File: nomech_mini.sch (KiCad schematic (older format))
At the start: 58 parts, among them CON1 USB_2B, CON2 AVR-ISP-6, P1 CONN_1, P2 CONN_1, P3 CONN_1, P4 CONN_1, P5 CONN_1, U1 ATMEGA32U4, X1 CRYSTAL_16MHz

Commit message: routing...
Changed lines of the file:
@@
-EESchema Schematic File Version 2  date Sat 04 May 2013 23:18:21 BST
+EESchema Schematic File Version 2  date Wed 08 May 2013 17:46:27 BST
 LIBS:power
 LIBS:device
@@
 Sheet 1 2
 Title ""
-Date "4 may 2013"
+Date "8 may 2013"
 Rev ""
 Comp ""
@@
 Text GLabel 4700 4050 1    60   Input ~ 0
 AN_1
+Text GLabel 5100 4050 1    60   Input ~ 0
+AN_2
 Text GLabel 4800 4050 1    60   Input ~ 0
-AN_2
-Text GLabel 4900 4050 1    60   Input ~ 0
 AN_3
-Text GLabel 5000 4050 1    60   Input ~ 0
+Text GLabel 5200 4050 1    60   Input ~ 0
 AN_4
 $Comp
@@
 Text GLabel 10750 5250 2    60   Input ~ 0
 Y2
-Text GLabel 5100 4050 1    60   Input ~ 0
+Text GLabel 4900 4050 1    60   Input ~ 0
 AN_5
-Text GLabel 5200 4050 1    60   Input ~ 0
+Text GLabel 6100 5100 2    60   Input ~ 0
 AN_6
-Text GLabel 6100 5200 2    60   Input ~ 0
+Text GLabel 5000 4050 1    60   Input ~ 0
 AN_7
 $Comp
@@
 Text GLabel 4100 6250 0    60   Output ~ 0
 SLOPE
-Text GLabel 6100 5100 2    60   Input ~ 0
+Text GLabel 6100 5200 2    60   Input ~ 0
 AN_8
 NoConn ~ 8050 5100

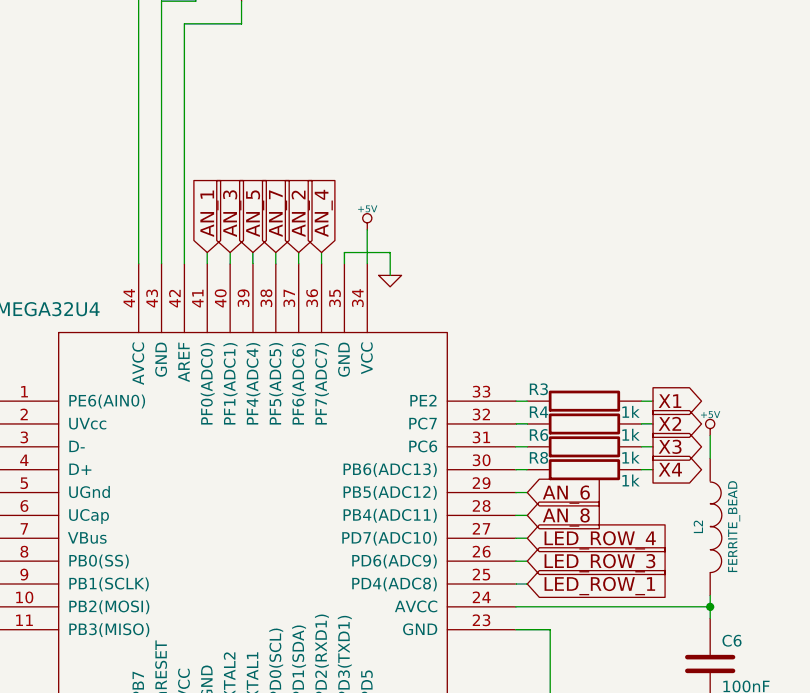
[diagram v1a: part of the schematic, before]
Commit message: routing, paying attention to looks on top layer
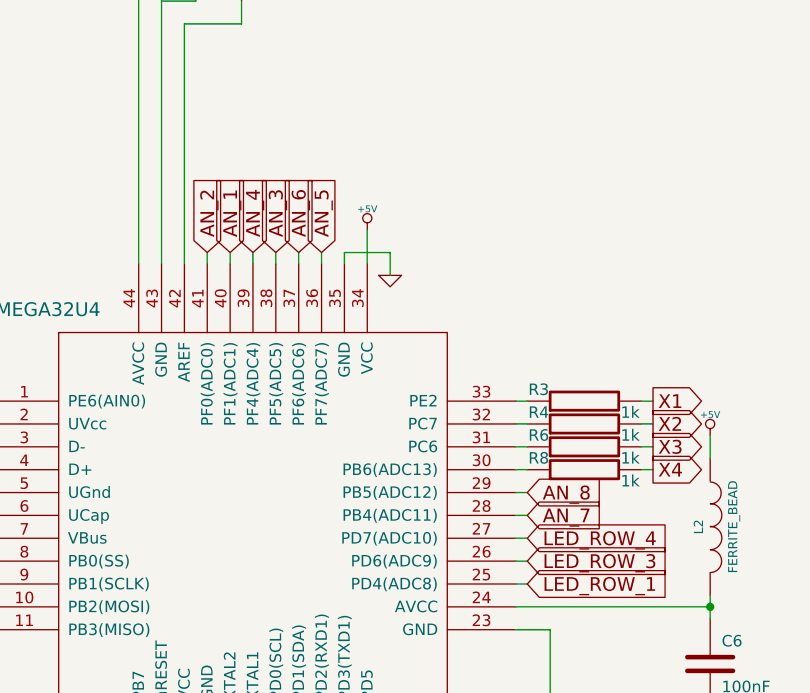
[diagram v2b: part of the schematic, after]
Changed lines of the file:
@@
-EESchema Schematic File Version 2  date Wed 08 May 2013 17:46:27 BST
+EESchema Schematic File Version 2
 LIBS:power
 LIBS:device
@@
 Sheet 1 2
 Title ""
-Date "8 may 2013"
+Date "29 may 2013"
 Rev ""
 Comp ""
@@
 Text GLabel 5650 6350 2    60   Input ~ 0
 LED_ROW_2
+Text GLabel 4800 4050 1    60   Input ~ 0
+AN_1
 Text GLabel 4700 4050 1    60   Input ~ 0
-AN_1
-Text GLabel 5100 4050 1    60   Input ~ 0
 AN_2
-Text GLabel 4800 4050 1    60   Input ~ 0
+Text GLabel 5000 4050 1    60   Input ~ 0
 AN_3
-Text GLabel 5200 4050 1    60   Input ~ 0
+Text GLabel 4900 4050 1    60   Input ~ 0
 AN_4
 $Comp
@@
 Text GLabel 10750 5250 2    60   Input ~ 0
 Y2
-Text GLabel 4900 4050 1    60   Input ~ 0
+Text GLabel 5200 4050 1    60   Input ~ 0
 AN_5
-Text GLabel 6100 5100 2    60   Input ~ 0
+Text GLabel 5100 4050 1    60   Input ~ 0
 AN_6
-Text GLabel 5000 4050 1    60   Input ~ 0
+Text GLabel 6100 5200 2    60   Input ~ 0
 AN_7
 $Comp
@@
 Text GLabel 4100 6250 0    60   Output ~ 0
 SLOPE
-Text GLabel 6100 5200 2    60   Input ~ 0
+Text GLabel 6100 5100 2    60   Input ~ 0
 AN_8
 NoConn ~ 8050 5100

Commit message: routing... ugly but nice
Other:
- moved on the sheet: R3, R4, R6, R8
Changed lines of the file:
@@
 	1    0    0    -1
 $EndComp
+Text GLabel 6650 5000 2    60   Output ~ 0
+X1
+Text GLabel 6650 4900 2    60   Output ~ 0
+X2
+Text GLabel 6650 4800 2    60   Output ~ 0
+X3
 Text GLabel 6650 4700 2    60   Output ~ 0
-X1
-Text GLabel 6650 4800 2    60   Output ~ 0
-X2
-Text GLabel 6650 4900 2    60   Output ~ 0
-X3
-Text GLabel 6650 5000 2    60   Output ~ 0
 X4
 $Comp
 L R R3
 U 1 1 5166EA72
-P 6350 4700
-F 0 "R3" V 6400 4900 50  0000 C CNN
-F 1 "1k" V 6300 4500 50  0000 C CNN
-F 2 "SM0805" H 6350 4700 60  0001 C CNN
-F 3 "" H 6350 4700 60  0000 C CNN
-	1    6350 4700
+P 6350 5000
+F 0 "R3" V 6400 5200 50  0000 C CNN
+F 1 "1k" V 6300 4800 50  0000 C CNN
+F 2 "SM0805" H 6350 5000 60  0001 C CNN
+F 3 "" H 6350 5000 60  0000 C CNN
+	1    6350 5000
 	0    -1   -1   0
 $EndComp
@@
 L R R4
 U 1 1 5166EA9E
+P 6350 4900
+F 0 "R4" V 6400 5100 50  0000 C CNN
+F 1 "1k" V 6300 4700 50  0000 C CNN
+F 2 "SM0805" H 6350 4900 60  0001 C CNN
+F 3 "" H 6350 4900 60  0000 C CNN
+	1    6350 4900
+	0    -1   -1   0
+$EndComp
+$Comp
+L R R6
+U 1 1 5166EAA4
 P 6350 4800
-F 0 "R4" V 6400 5000 50  0000 C CNN
+F 0 "R6" V 6400 5000 50  0000 C CNN
 F 1 "1k" V 6300 4600 50  0000 C CNN
 F 2 "SM0805" H 6350 4800 60  0001 C CNN
@@
 $EndComp
 $Comp
-L R R6
-U 1 1 5166EAA4
-P 6350 4900
-F 0 "R6" V 6400 5100 50  0000 C CNN
-F 1 "1k" V 6300 4700 50  0000 C CNN
-F 2 "SM0805" H 6350 4900 60  0001 C CNN
-F 3 "" H 6350 4900 60  0000 C CNN
-	1    6350 4900
-	0    -1   -1   0
-$EndComp
-$Comp
 L R R8
 U 1 1 5166EAAA
-P 6350 5000
-F 0 "R8" V 6400 5200 50  0000 C CNN
-F 1 "1k" V 6300 4800 50  0000 C CNN
-F 2 "SM0805" H 6350 5000 60  0001 C CNN
-F 3 "" H 6350 5000 60  0000 C CNN
-	1    6350 5000
+P 6350 4700
+F 0 "R8" V 6400 4900 50  0000 C CNN
+F 1 "1k" V 6300 4500 50  0000 C CNN
+F 2 "SM0805" H 6350 4700 60  0001 C CNN
+F 3 "" H 6350 4700 60  0000 C CNN
+	1    6350 4700
 	0    -1   -1   0
 $EndComp
@@
 	4200 6350 4400 6350
 Wire Wire Line
-	6050 5000 6100 5000
-Wire Wire Line
-	6050 4900 6100 4900
-Wire Wire Line
-	6050 4800 6100 4800
-Wire Wire Line
-	6050 4700 6100 4700
+	6600 5000 6650 5000
+Wire Wire Line
+	6600 4900 6650 4900
+Wire Wire Line
+	6600 4800 6650 4800
 Wire Wire Line
 	6600 4700 6650 4700
-Wire Wire Line
-	6600 4800 6650 4800
-Wire Wire Line
-	6600 4900 6650 4900
-Wire Wire Line
-	6600 5000 6650 5000
 Connection ~ 3700 9900
 Wire Wire Line
@@
 Connection ~ 15100 6400
 Connection ~ 15100 6900
+Wire Wire Line
+	6050 4700 6100 4700
+Wire Wire Line
+	6050 4800 6100 4800
+Wire Wire Line
+	6050 4900 6100 4900
+Wire Wire Line
+	6050 5000 6100 5000
 $EndSCHEMATC

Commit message: routing... nicely
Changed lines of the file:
@@
 Text Label 3750 5500 2    60   ~ 0
 ISP_SCK
+Text GLabel 6500 6350 2    60   Input ~ 0
+LED_COLUMN_1
+Text GLabel 6500 6500 2    60   Input ~ 0
+LED_COLUMN_2
+Text GLabel 6500 6650 2    60   Input ~ 0
+LED_COLUMN_3
 Text GLabel 6500 6800 2    60   Input ~ 0
-LED_COLUMN_1
-Text GLabel 6500 6650 2    60   Input ~ 0
-LED_COLUMN_2
-Text GLabel 6500 6500 2    60   Input ~ 0
-LED_COLUMN_3
-Text GLabel 6500 6350 2    60   Input ~ 0
 LED_COLUMN_4
 Text GLabel 6100 5500 2    60   Input ~ 0

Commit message: routing.. SPI done
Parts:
- added C19: 100nF, SM0805, symbol C
- added C20: 10nF, SM0805, symbol C
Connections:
- wire segments 177 -> 181
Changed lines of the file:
@@
 Sheet 1 2
 Title ""
-Date "29 may 2013"
+Date "30 may 2013"
 Rev ""
 Comp ""
@@
 	1    0    0    -1
 $EndComp
+$Comp
+L C C19
+U 1 1 51A71665
+P 2500 9650
+F 0 "C19" H 2540 9674 70  0000 L BNN
+F 1 "100nF" H 2539 9485 70  0000 L BNN
+F 2 "SM0805" H 2539 9585 70  0001 C CNN
+F 3 "" H 2500 9650 60  0001 C CNN
+	1    2500 9650
+	1    0    0    -1
+$EndComp
 Wire Wire Line
 	2100 5050 2150 5050
@@
 Connection ~ 3450 9400
 Wire Wire Line
-	2950 9400 4550 9400
+	2500 9400 4950 9400
 Connection ~ 4050 9400
 Wire Wire Line
@@
 Connection ~ 3700 9400
 Wire Wire Line
-	2950 9900 4550 9900
+	2500 9900 4950 9900
 Connection ~ 4050 9900
 Wire Wire Line
@@
 Wire Wire Line
 	6050 5000 6100 5000
+Wire Wire Line
+	2500 9450 2500 9400
+Connection ~ 2950 9400
+Wire Wire Line
+	2500 9850 2500 9900
+Connection ~ 2950 9900
+$Comp
+L C C20
+U 1 1 51A71989
+P 4950 9650
+F 0 "C20" H 4990 9674 70  0000 L BNN
+F 1 "10nF" H 4989 9485 70  0000 L BNN
+F 2 "SM0805" H 4989 9585 70  0001 C CNN
+F 3 "" H 4950 9650 60  0001 C CNN
+	1    4950 9650
+	1    0    0    -1
+$EndComp
+Wire Wire Line
+	4950 9400 4950 9450
+Connection ~ 4550 9400
+Wire Wire Line
+	4950 9900 4950 9850
+Connection ~ 4550 9900
 $EndSCHEMATC

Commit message: routing, grounds on outside
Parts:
- removed P1, P2, P3, P5: CONN_1, PIN_ARRAY_1, symbol CONN_1
- added GND1, VCC1: TEST, symbol TEST
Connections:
- wire segments 181 -> 184
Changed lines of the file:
@@
 Sheet 1 2
 Title ""
-Date "30 may 2013"
+Date "4 jun 2013"
 Rev ""
 Comp ""
@@
 $EndComp
 $Comp
-L CONN_1 P1
-U 1 1 5167682C
-P 10700 3750
-F 0 "P1" H 10780 3750 40  0000 L CNN
-F 1 "CONN_1" H 10700 3805 30  0001 C CNN
-F 2 "PIN_ARRAY_1" H 10700 3750 60  0001 C CNN
-F 3 "" H 10700 3750 60  0000 C CNN
-	1    10700 3750
-	0    -1   -1   0
-$EndComp
-$Comp
-L CONN_1 P2
-U 1 1 51676929
-P 10700 5050
-F 0 "P2" H 10780 5050 40  0000 L CNN
-F 1 "CONN_1" H 10700 5105 30  0001 C CNN
-F 2 "PIN_ARRAY_1" H 10700 5050 60  0001 C CNN
-F 3 "" H 10700 5050 60  0000 C CNN
-	1    10700 5050
-	0    -1   -1   0
-$EndComp
-$Comp
-L CONN_1 P3
-U 1 1 51676A17
-P 10700 6400
-F 0 "P3" H 10780 6400 40  0000 L CNN
-F 1 "CONN_1" H 10700 6455 30  0001 C CNN
-F 2 "PIN_ARRAY_1" H 10700 6400 60  0001 C CNN
-F 3 "" H 10700 6400 60  0000 C CNN
-	1    10700 6400
-	0    -1   -1   0
-$EndComp
-$Comp
-L CONN_1 P5
-U 1 1 51676B07
-P 10700 7750
-F 0 "P5" H 10780 7750 40  0000 L CNN
-F 1 "CONN_1" H 10700 7805 30  0001 C CNN
-F 2 "PIN_ARRAY_1" H 10700 7750 60  0001 C CNN
-F 3 "" H 10700 7750 60  0000 C CNN
-	1    10700 7750
-	0    -1   -1   0
-$EndComp
-$Comp
 L +5V #PWR019
 U 1 1 51677795
@@
 Wire Wire Line
 	2350 6500 2400 6500
-Wire Wire Line
-	10700 3900 10700 3950
-Connection ~ 10700 3950
-Wire Wire Line
-	10700 5200 10700 5250
-Connection ~ 10700 5250
-Wire Wire Line
-	10700 6550 10700 6600
-Connection ~ 10700 6600
-Wire Wire Line
-	10700 7900 10700 7950
-Connection ~ 10700 7950
 Wire Wire Line
 	4050 9450 4050 9400
@@
 	4950 9900 4950 9850
 Connection ~ 4550 9900
+$Comp
+L GND #PWR024
+U 1 1 51AE26F0
+P 1750 8250
+F 0 "#PWR024" H 1750 8250 30  0001 C CNN
+F 1 "GND" H 1750 8180 30  0001 C CNN
+F 2 "" H 1750 8250 60  0001 C CNN
+F 3 "" H 1750 8250 60  0001 C CNN
+	1    1750 8250
+	1    0    0    -1
+$EndComp
+$Comp
+L +5V #PWR025
+U 1 1 51AE280D
+P 2300 7950
+F 0 "#PWR025" H 2300 8040 20  0001 C CNN
+F 1 "+5V" H 2300 8040 30  0000 C CNN
+F 2 "" H 2300 7950 60  0000 C CNN
+F 3 "" H 2300 7950 60  0000 C CNN
+	1    2300 7950
+	1    0    0    -1
+$EndComp
+$Comp
+L TEST GND1
+U 1 1 51AE2809
+P 1750 8100
+F 0 "GND1" H 1750 8160 40  0000 C CNN
+F 1 "TEST" H 1750 8030 40  0000 C CNN
+F 2 "" H 1750 8100 60  0000 C CNN
+F 3 "" H 1750 8100 60  0000 C CNN
+	1    1750 8100
+	1    0    0    -1
+$EndComp
+Wire Wire Line
+	1550 8100 1550 8200
+Wire Wire Line
+	1550 8200 1950 8200
+Wire Wire Line
+	1950 8200 1950 8100
+Wire Wire Line
+	1750 8200 1750 8250
+Connection ~ 1750 8200
+$Comp
+L TEST VCC1
+U 1 1 51AE2A39
+P 2300 8100
+F 0 "VCC1" H 2300 8160 40  0000 C CNN
+F 1 "TEST" H 2300 8030 40  0000 C CNN
+F 2 "" H 2300 8100 60  0000 C CNN
+F 3 "" H 2300 8100 60  0000 C CNN
+	1    2300 8100
+	1    0    0    -1
+$EndComp
+Wire Wire Line
+	2100 8100 2100 7950
+Wire Wire Line
+	2100 7950 2500 7950
+Wire Wire Line
+	2500 7950 2500 8100
+Connection ~ 2300 7950
 $EndSCHEMATC

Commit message: trying to sort out the dual atmega libs
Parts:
- U1: value ATMEGA32U4 -> ATMEGA32U4_2; symbol ATMEGA32U4 -> ATMEGA32U4_2
